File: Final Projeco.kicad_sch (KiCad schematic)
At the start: 9 parts, among them SW1 SW_Omron_B3FS, SW2 SW_Omron_B3FS, U1 ESP32-S3, U2 GT-USB-7004N, X1 TZ1269D

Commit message: -Updated some parts -added datasheets for possible Antanneax -design is structurally complete... I think?
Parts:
- added C4, C5, C6: C, Capacitor_SMD:C_0402_1005Metric, symbol Device:C
- added JP1: U_FL-R-SMT-1(10), jlc:ANT-SMD_UFL-R-SMT-1-10, symbol jlc:U_FL-R-SMT-1(10)
- added R2, R3, R4: R, Resistor_SMD:R_0402_1005Metric, symbol Device:R
- added U3: NCP167BMX330TBG, jlc:XDFN-4_L1.0-W1.0-P0.65-BL-EP, symbol jlc:NCP167BMX330TBG
- C1, C2, C3: footprint (none) -> Capacitor_SMD:C_0402_1005Metric
- R1: footprint (none) -> Resistor_SMD:R_0402_1005Metric
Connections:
- net GND: now also U2.A1B12 (GND), U2.B1A12 (GND), C4.2, C5.2, C6.2, JP1.1 (GND), JP1.3 (GND), R2.2, R3.2, U3.2 (GND), U3.5 (EPAD)
- net at U1.1 (LNA_IN/RF): now also JP1.2 (SIN)
- net at U1.25 (GPIO19/USB_D-/ADC2_CH8): now also U2.A7 (DN1), U2.B7 (DN2)
- net at U1.26 (GPIO20/USB_D+/ADC2_CH9): now also U2.A6 (DP1), U2.B6 (DP2)
- net at U1.55 (VDDA), U1.56 (VDDA): now also C5.1, U3.1 (OUT)
- net at U1.57 (GND): now also C4.1
- net at U2.A4B9 (VBUS): now also U2.B4A9 (VBUS), R4.1
- net at U2.A5 (CC1): now also R3.1
- net at U2.B5 (CC2): now also R2.1
- new net: C6.1, R4.2, U3.3 (EN), U3.4 (IN)
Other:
- moved on the sheet: C1, C2, C3, R1, SW1, SW2, U1, U2, X1

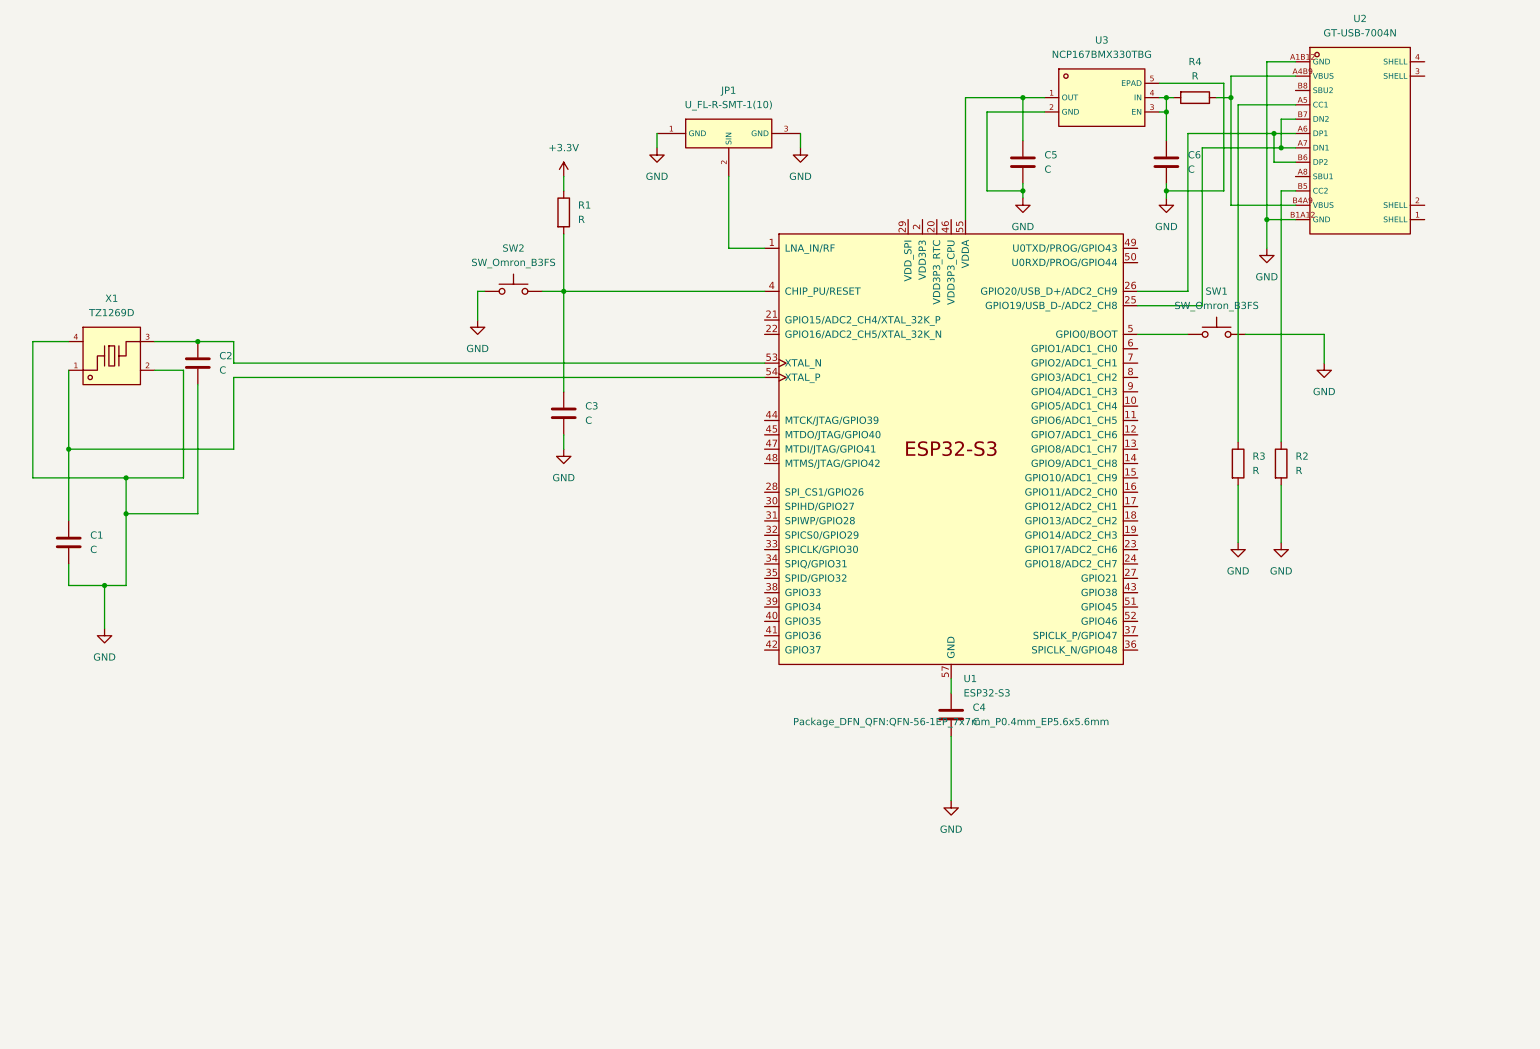
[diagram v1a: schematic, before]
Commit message: -Cleaned up schematic (Nets) -Added more Deditated wam
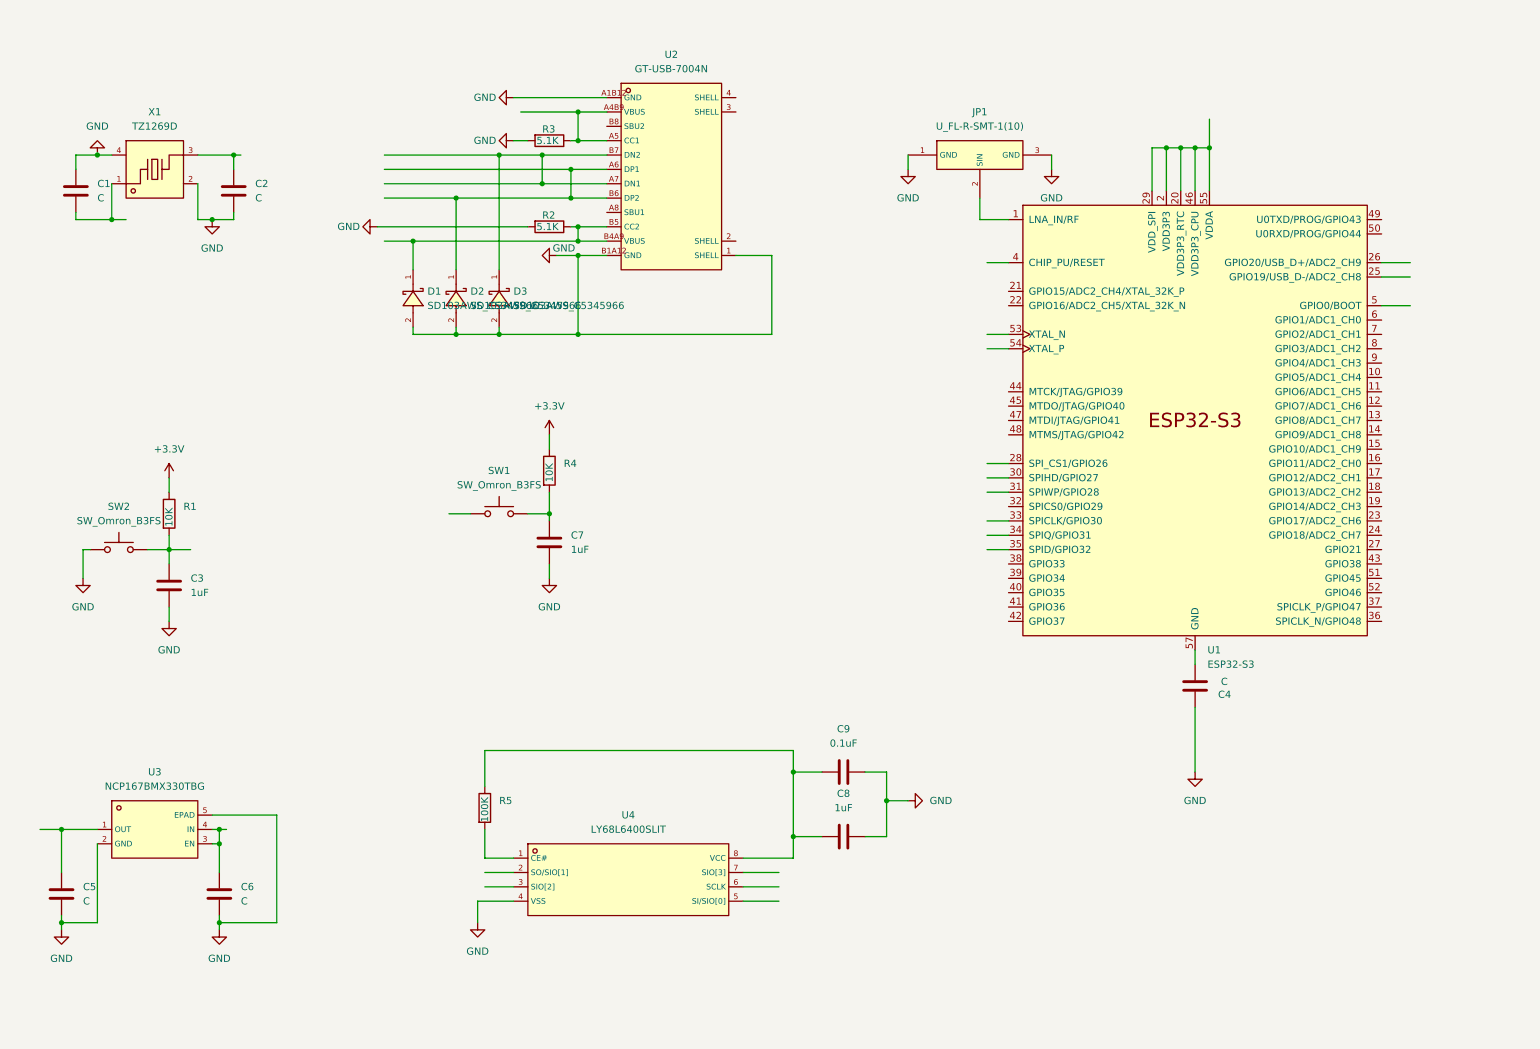
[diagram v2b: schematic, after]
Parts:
- added C7, C8: 1uF, Capacitor_SMD:C_0402_1005Metric, symbol Device:C
- added C9: 0.1uF, Capacitor_SMD:C_0402_1005Metric, symbol Device:C
- added D1, D2, D3: SD103AWS_C5345966, jlc:SOD-323_L1.7-W1.3-LS2.5-RD, symbol jlc:SD103AWS_C5345966
- added R5: 100K, Resistor_SMD:R_0402_1005Metric, symbol Device:R
- added U4: LY68L6400SLIT, jlc:SOP-8_L4.9-W3.9-P1.27-LS6.0-BL, symbol jlc:LY68L6400SLIT
- C3: value C -> 1uF
- R1, R4: value R -> 10K
- R2, R3: value R -> 5.1K
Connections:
- net +3.3V: now also R4.1
- net GND: now also C1.1, U2.1 (SHELL), C7.2, C8.2, C9.2, D1.2 (A), D2.2 (A), D3.2 (A), U4.4 (VSS); no longer C1.2, SW1.2
- net VDD3P3: now also U1.20 (VDD3P3_RTC), U1.29 (VDD_SPI), U1.46 (VDD3P3_CPU), U1.55 (VDDA), U1.56 (VDDA)
- net at C6.1, U3.3 (EN), U3.4 (IN): no longer R4.2
- net at U2.A7 (DN1), U2.B7 (DN2): now also D3.1 (K); no longer U1.25 (GPIO19/USB_D-/ADC2_CH8)
- net at U2.A6 (DP1), U2.B6 (DP2): now also D2.1 (K); no longer U1.26 (GPIO20/USB_D+/ADC2_CH9)
- net at C3.1, R1.2, SW2.2: no longer U1.4 (CHIP_PU/RESET)
- net at U1.5 (GPIO0/BOOT): no longer SW1.1
- net at C2.1, X1.3: no longer U1.53 (XTAL_N)
- net at C5.1, U3.1 (OUT): no longer U1.55 (VDDA), U1.56 (VDDA)
- net at R3.1, U2.A5 (CC1): now also U2.A4B9 (VBUS)
- net at R2.1, U2.B5 (CC2): now also U2.B4A9 (VBUS), D1.1 (K)
- new net: C1.2, X1.1
- new net: C7.1, R4.2, SW1.2
- new net: C8.1, C9.1, R5.1, U4.8 (VCC)
- new net: R5.2, U4.1 (CE#)
- now unconnected: U1.54 (XTAL_P)
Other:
- title: (none) -> ENGR342 PCB Design
- moved on the sheet: C2, C3, C4, C5, C6, JP1, R1, R3, SW2, U1, U2, U3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

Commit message: -USE IPEX 2.4 GHz Antenna
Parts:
- U1: LCSC (none) -> C291392
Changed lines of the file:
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@@
+			)
+		)
+		(property "LCSC" "C291392"
+			(at 226.06 85.09 0)
+			(effects
+				(font
+					(size 1.27 1.27)
+				)
+				(hide yes)
 			)
 		)

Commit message: Fixed all the traces to connect to each other :-|
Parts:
- removed SW1, SW2: SW_Omron_B3FS, symbol Switch:SW_Omron_B3FS
- added U5, U6: PTS830GG140SMTRLFS, jlc:KEY-SMD_4P-L3.1-W2.6_PTS830GG140SMTRLFS, symbol jlc:PTS830GG140SMTRLFS
- added U7: 220S-2*16P_H=8_5MM_Ytype_L=3_0MM_PBT, jlc:HDR-TH_32P-P2.54-V-F-R2-C16-S2.54, symbol LC:220S-2*16P_H=8_5MM_Ytype_L=3_0MM_PBT
- C4: value C -> 1u
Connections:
- net GND: now also U5.3, U7.2
- net VDD3P3: now also C5.1, U3.1 (OUT), U7.1
- net XTAL_P: now reaches C1.2, X1.1
- net XTAL_P: now also U1.53 (XTAL_N)
- net VBUS: now reaches D1.1 (K), R2.1, U2.B4A9 (VBUS), U2.B5 (CC2)
- net VBUS: now also C6.1, R3.1, U2.A4B9 (VBUS), U2.A5 (CC1), U3.3 (EN), U3.4 (IN)
- net GPIO5: now reaches U1.10 (GPIO5/ADC1_CH4)
- net GPIO5: now also U7.16
- net GPIO6: now reaches U1.11 (GPIO6/ADC1_CH5)
- net GPIO6: now also U7.18
- net GPIO7: now reaches U1.12 (GPIO7/ADC1_CH6)
- net GPIO7: now also U7.20
- net GPIO8: now reaches U1.13 (GPIO8/ADC1_CH7)
- net GPIO8: now also U7.22
- net GPIO9: now reaches U1.14 (GPIO9/ADC1_CH8)
- net GPIO9: now also U7.24
- net GPIO10: now reaches U1.15 (GPIO10/ADC1_CH9)
- net GPIO10: now also U7.26
- net GPIO11: now reaches U1.16 (GPIO11/ADC2_CH0)
- net GPIO11: now also U7.28
- net GPIO12: now reaches U1.17 (GPIO12/ADC2_CH1)
- net GPIO12: now also U7.30
- net GPIO13: now reaches U1.18 (GPIO13/ADC2_CH2)
- net GPIO13: now also U7.32
- net GPIO14: now reaches U1.19 (GPIO14/ADC2_CH3)
- net GPIO14: now also U7.3
- net GPIO17: now reaches U1.23 (GPIO17/ADC2_CH6)
- net GPIO17: now also U7.5
- net GPIO18: now reaches U1.24 (GPIO18/ADC2_CH7)
- net GPIO18: now also U7.7
- net USB_D+: now reaches U1.25 (GPIO19/USB_D-/ADC2_CH8)
- net USB_D+: now also D2.1 (K), U2.A6 (DP1), U2.B6 (DP2)
- net USB_D-: now reaches U1.26 (GPIO20/USB_D+/ADC2_CH9)
- net USB_D-: now also D3.1 (K), U2.A7 (DN1), U2.B7 (DN2)
- net GPIO21: now reaches U1.27 (GPIO21)
- net GPIO21: now also U7.9
- net SPICS1: now reaches U1.28 (SPI_CS1/GPIO26)
- net SPICS1: now also R5.2, U4.1 (CE#)
- net SPIHD: now reaches U1.30 (SPIHD/GPIO27)
- net SPIHD: now also U4.7 (SIO[3])
- net SPIWP: now reaches U1.31 (SPIWP/GPIO28)
- net SPIWP: now also U4.3 (SIO[2])
- net SPICLK: now reaches U1.33 (SPICLK/GPIO30)
- net SPICLK: now also U4.6 (SCLK)
- net SPIQ: now reaches U1.34 (SPIQ/GPIO31)
- net SPIQ: now also U4.2 (SO/SIO[1])
- net SPID: now reaches U1.35 (SPID/GPIO32)
- net SPID: now also U4.5 (SI/SIO[0])
- net RESET: now reaches U1.4 (CHIP_PU/RESET)
- net RESET: now also C3.1, R1.2, U5.2
- net GPIO38: now reaches U1.43 (GPIO38)
- net GPIO38: now also U7.11
- net GPIO0/BOOT: now reaches U1.5 (GPIO0/BOOT)
- net GPIO0/BOOT: now also U6.3, U7.4
- net GPIO45: now reaches U1.51 (GPIO45)
- net GPIO45: now also U7.13
- net GPIO46: now reaches U1.52 (GPIO46)
- net GPIO46: now also U7.15
- net XTAL_N: now reaches U1.54 (XTAL_P)
- net XTAL_N: now also C2.1, X1.3
- net GPIO1: now reaches U1.6 (GPIO1/ADC1_CH0)
- net GPIO1: now also U7.6
- net GPIO2: now reaches U1.7 (GPIO2/ADC1_CH1)
- net GPIO2: now also U7.8
- net GPIO3: now reaches U1.8 (GPIO3/ADC1_CH2)
- net GPIO3: now also U7.10, U7.12
- net GPIO4: now reaches U1.9 (GPIO4/ADC1_CH3)
- net GPIO4: now also U7.14
- net at C7.1, R4.2: now also U6.2
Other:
- moved on the sheet: C3, C4, C5, C6, C7, C8, C9, JP1, R1, R4, R5, U1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

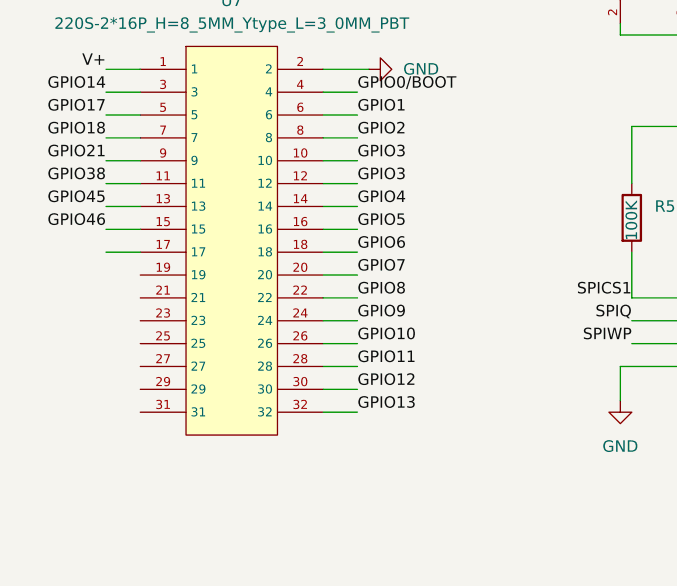
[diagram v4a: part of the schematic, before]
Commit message: Fixed some stuff
-added diff pair net rules
-added base net rules
-added zmatch net rules
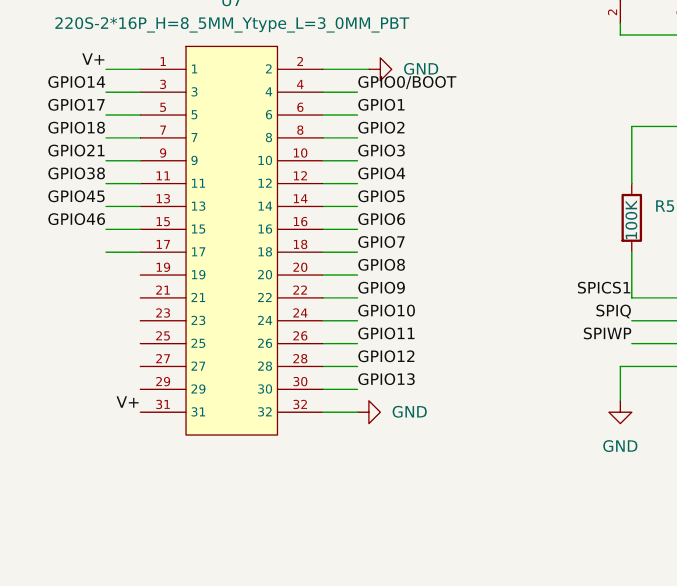
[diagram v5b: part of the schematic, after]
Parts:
- U1: LCSC C291392 -> C2913194
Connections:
- net GND: now also U7.32
- net GPIO10: now also U7.24; no longer U7.26
- net GPIO11: now also U7.26; no longer U7.28
- net GPIO12: now also U7.28; no longer U7.30
- net GPIO13: now also U7.30; no longer U7.32
- net GPIO3: no longer U7.12
- net GPIO4: now also U7.12; no longer U7.14
- net GPIO5: now also U7.14; no longer U7.16
- net GPIO6: now also U7.16; no longer U7.18
- net GPIO7: now also U7.18; no longer U7.20
- net GPIO8: now also U7.20; no longer U7.22
- net GPIO9: now also U7.22; no longer U7.24
- net VDD3P3: now also U7.31

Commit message: Started Routing
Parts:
- C3, C7: LCSC (none) -> C961495
- C4: value 1u -> 1uF
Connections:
- net +3.3V is gone; now on net VDD3P3: R1.1, R4.1
- net GPIO0/BOOT: now also U7.6; no longer U7.4
- net GPIO1: now also U7.8; no longer U7.6
- net GPIO10: now also U7.26; no longer U7.24
- net GPIO11: now also U7.28; no longer U7.26
- net GPIO12: now also U7.1; no longer U7.28
- net GPIO13: now also U7.3; no longer U7.30
- net GPIO14: now also U7.5; no longer U7.3
- net GPIO17: now also U7.11; no longer U7.5
- net GPIO18: now also U7.13; no longer U7.7
- net GPIO2: now also U7.10; no longer U7.8
- net GPIO21: now also U7.15; no longer U7.9
- net GPIO3: now also U7.12; no longer U7.10
- net GPIO38: now also U7.17; no longer U7.11
- net GPIO4: now also U7.14; no longer U7.12
- net GPIO45: now also U7.19; no longer U7.13
- net GPIO46: now also U7.21; no longer U7.15
- net GPIO5: now also U7.16; no longer U7.14
- net GPIO6: now also U7.18; no longer U7.16
- net GPIO7: now also U7.20; no longer U7.18
- net GPIO8: now also U7.22; no longer U7.20
- net GPIO9: now also U7.24; no longer U7.22
- net VDD3P3: now also U7.30, U7.4; no longer U7.1, U7.31
- net GPIO15: now reaches U1.21 (GPIO15/ADC2_CH4/XTAL_32K_P)
- net GPIO15: now also U7.7
- net GPIO16: now reaches U1.22 (GPIO16/ADC2_CH5/XTAL_32K_N)
- net GPIO16: now also U7.9
- net GPIO33: now reaches U1.38 (GPIO33)
- net GPIO33: now also U7.23
- net GPIO34: now reaches U1.39 (GPIO34)
- net GPIO34: now also U7.25
- net GPIO35: now reaches U1.40 (GPIO35)
- net GPIO35: now also U7.27
- net GPIO36: now reaches U1.41 (GPIO36)
- net GPIO36: now also U7.29
- net GPIO37: now reaches U1.42 (GPIO37)
- net GPIO37: now also U7.31
- no-connect marks 0 -> 18

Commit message: stuff
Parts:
- added C10: 1uF, Capacitor_SMD:C_0402_1005Metric, symbol Device:C
- added R6: 442k, Resistor_SMD:R_0402_1005Metric, symbol Device:R
- C1, C2: value C -> 13pF; LCSC (none) -> C161528
- C3, C7: LCSC C961495 -> C29266
- C4, C8: LCSC (none) -> C29266
- C5, C6: value C -> 1uF; LCSC (none) -> C29266
- C9: LCSC (none) -> C307331
- R1, R4: LCSC (none) -> C25744
- R2, R3: LCSC (none) -> C14677
- R5: LCSC (none) -> C25741
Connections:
- net GND: now also U2.2 (SHELL), U2.3 (SHELL), U2.4 (SHELL), C10.2, R6.2
- net SPICLK_GPIO47: now reaches U1.37 (SPICLK_P/GPIO47)
- net SPICLK_GPIO47: now also C10.1, R6.1
- net GND_PIN: now reaches C4.1, U1.57 (GND)
- no-connect marks 18 -> 14
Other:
- moved on the sheet: C4
